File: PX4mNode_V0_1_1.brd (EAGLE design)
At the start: 48.6 x 34.9 mm, 134 parts, among them J201 DF13C-6P-1.25V, J202 DF13C-6P-1.25V, J203 DF13C-6P-1.25V, J301 DF13C-4P-1.25V, J401 DF13C-7P-1.25V, J402 DF13-4P-1.25V, J403 DF13C-4P-1.25V, J404 DF13C-4P-1.25V, J405 DF13C-4P-1.25V, J801 DF13C-3P-1.25V, M3_MOUNT1101 MOUNT-HOLE3.1MM, M3_MOUNT1102 MOUNT-HOLE3.1MM, M3_MOUNT1103 MOUNT-HOLE3.1MM, M3_MOUNT1104 MOUNT-HOLE3.1MM, U101 STM32F4X7VX, U401 MAX3051, U402 MAX3051, X101 3.2x2.5 mm / 24 MHz / 15 ppm

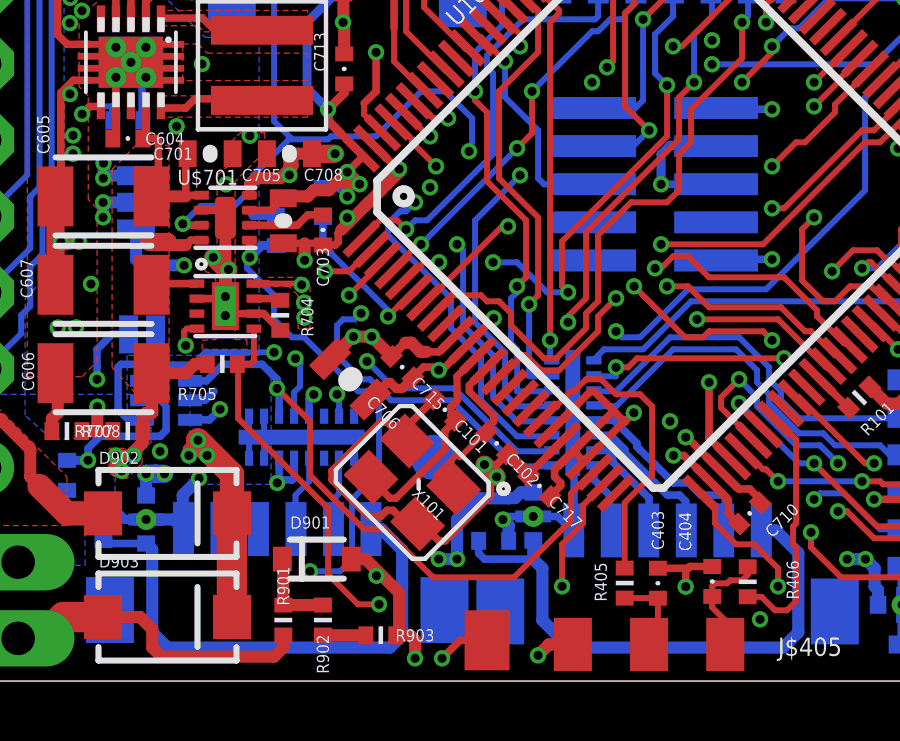
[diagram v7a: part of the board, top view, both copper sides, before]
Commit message: Reworked VBAT pullup to make psace around PSU
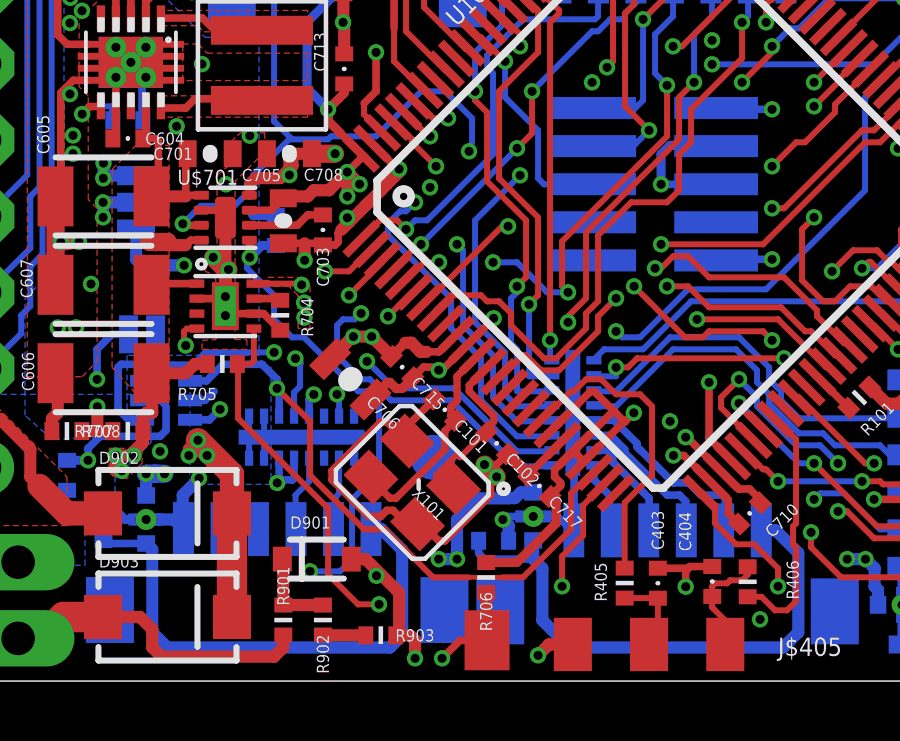
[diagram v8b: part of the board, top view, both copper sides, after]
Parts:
- moved R706 13.6 mm to (32.7, 6.19), flipped to the top
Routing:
- net FMU-VDD_3V3: track 130.4 -> 133.4 mm
- net VBAT: track 19.4 -> 16.7 mm
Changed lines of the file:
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@@
 <layer number="1" name="Top" color="4" fill="1" visible="yes" active="yes"/>
 <layer number="2" name="Ground" color="2" fill="10" visible="no" active="yes"/>
-<layer number="3" name="Horizontal" color="13" fill="15" visible="yes" active="yes"/>
+<layer number="3" name="Horizontal" color="13" fill="15" visible="no" active="yes"/>
 <layer number="4" name="Route4" color="1" fill="4" visible="no" active="no"/>
 <layer number="5" name="Route5" color="4" fill="4" visible="no" active="no"/>
@@
 <layer number="12" name="Route12" color="1" fill="5" visible="no" active="no"/>
 <layer number="13" name="Route13" color="4" fill="5" visible="no" active="no"/>
-<layer number="14" name="Vertical" color="14" fill="15" visible="yes" active="yes"/>
+<layer number="14" name="Vertical" color="14" fill="15" visible="no" active="yes"/>
 <layer number="15" name="Power" color="11" fill="15" visible="no" active="yes"/>
 <layer number="16" name="Bottom" color="1" fill="1" visible="yes" active="yes"/>
@@
 <attribute name="PARTNO" value="DF13C-4P-1.25V(20)" x="47.0408" y="33.528" size="1.778" layer="28" rot="MR180" display="off"/>
 </element>
-<element name="R706" library="pixhawk2" package="0402-RES" value="1K" x="27.2288" y="18.6944" rot="MR90">
-<attribute name="PARTNO" value="RC0402FR-071KL" x="27.2288" y="18.6944" size="1.778" layer="28" rot="MR90" display="off"/>
+<element name="R706" library="pixhawk2" package="0402-RES" value="1K" x="32.6712" y="6.1944" rot="R90">
+<attribute name="PARTNO" value="RC0402FR-071KL" x="32.6712" y="6.1944" size="1.778" layer="27" rot="R90" display="off"/>
 </element>
 <element name="C703" library="pixhawk2" package="0402-CAP" value="10n" x="27.2288" y="17.78" rot="R90">
@@
 <wire x1="35.56" y1="30.5816" x2="38.2016" y2="30.5816" width="0.4064" layer="1"/>
 <wire x1="38.2016" y1="30.5816" x2="38.2016" y2="30.6832" width="0.4064" layer="1"/>
-<wire x1="27.2288" y1="19.1944" x2="27.7448" y2="19.1944" width="0.254" layer="16"/>
-<wire x1="27.7448" y1="19.1944" x2="28.0416" y2="18.8976" width="0.254" layer="16"/>
 <wire x1="39.7256" y1="36.6776" x2="40.0304" y2="36.9824" width="0.6096" layer="1"/>
 <wire x1="40.0304" y1="36.9824" x2="40.132" y2="36.9824" width="0.6096" layer="1"/>
@@
 <wire x1="25.5" y1="22.8" x2="26.5" y2="21.8" width="0.254" layer="14"/>
 <wire x1="26.5" y1="21.8" x2="27.4" y2="21.8" width="0.254" layer="14"/>
-<wire x1="21.8" y1="10.9" x2="21.8" y2="10.4" width="0" layer="19" extent="16-16"/>
+<wire x1="21.8" y1="10.4" x2="21.8" y2="10.9" width="0" layer="19" extent="16-16"/>
+<wire x1="32.6712" y1="6.6944" x2="33.6944" y2="6.6944" width="0.3048" layer="1"/>
+<wire x1="33.6944" y1="6.6944" x2="35" y2="8" width="0.3048" layer="1"/>
+<wire x1="35" y1="8" x2="35" y2="8.687996875" width="0.3048" layer="1"/>
+<wire x1="35" y1="8.687996875" x2="34.795953125" y2="8.89204375" width="0.3048" layer="1"/>
 </signal>
 <signal name="OTG_FS_DP">
@@
 <contactref element="R706" pad="P$1"/>
 <wire x1="29.4" y1="14.9" x2="30.2" y2="15.7" width="0.2" layer="1"/>
-<wire x1="27.5" y1="17" x2="29.4" y2="15.1" width="0.2" layer="16"/>
-<wire x1="29.4" y1="15.1" x2="29.4" y2="14.9" width="0.2" layer="16"/>
 <wire x1="30.2" y1="15.7" x2="30.273071875" y2="15.71561875" width="0.2" layer="1"/>
-<wire x1="27.3" y1="18.2" x2="27.2288" y2="18.1944" width="0.2" layer="16"/>
 <via x="29.4" y="14.9" extent="1-16" drill="0.3" diameter="0.55"/>
 <contactref element="JP701" pad="P$1"/>
@@
 <wire x1="29.4" y1="14.9" x2="29.7" y2="14.6" width="0.254" layer="14"/>
 <via x="31.2" y="3.5" extent="1-16" drill="0.3"/>
-<wire x1="27.5" y1="17" x2="27.2288" y2="17.2712" width="0.254" layer="16"/>
-<wire x1="27.2288" y1="17.2712" x2="27.2288" y2="18.1944" width="0.254" layer="16"/>
+<wire x1="32.6712" y1="5.6944" x2="32.6712" y2="4.1288" width="0.4064" layer="1"/>
+<wire x1="32.6712" y1="4.1288" x2="32.7" y2="4.1" width="0.4064" layer="1"/>
 </signal>
 <signal name="N$11">
@@
 <wire x1="35.2" y1="8.7" x2="32.3" y2="11.6" width="0.2" layer="14"/>
 <wire x1="35.2" y1="5.9" x2="35.2" y2="8.7" width="0.2" layer="14"/>
-<wire x1="35.2" y1="7.3" x2="35.2" y2="5.9" width="0.2" layer="1"/>
-<wire x1="35.9" y1="8" x2="35.2" y2="7.3" width="0.2" layer="1"/>
-<wire x1="35.9" y1="8.6" x2="35.9" y2="8" width="0.2" layer="1"/>
+<wire x1="35.2" y1="6.9" x2="35.2" y2="5.9" width="0.2" layer="1"/>
+<wire x1="35.9" y1="7.6" x2="35.2" y2="6.9" width="0.2" layer="1"/>
+<wire x1="35.9" y1="8.6" x2="35.9" y2="7.6" width="0.2" layer="1"/>
 <wire x1="36.6" y1="9.3" x2="35.9" y2="8.6" width="0.2" layer="1"/>
 <wire x1="23.1" y1="28.1" x2="23.0632" y2="28.1432" width="0.2" layer="16"/>
@@
 <wire x1="29.3" y1="7.8" x2="28.6" y2="7.8" width="0.2" layer="1"/>
 <wire x1="30.9" y1="6.2" x2="29.3" y2="7.8" width="0.2" layer="1"/>
-<wire x1="33.6" y1="6.2" x2="30.9" y2="6.2" width="0.2" layer="1"/>
-<wire x1="35.5" y1="8.1" x2="33.6" y2="6.2" width="0.2" layer="1"/>
-<wire x1="35.5" y1="9" x2="35.5" y2="8.1" width="0.2" layer="1"/>
+<wire x1="33.9" y1="6.2" x2="33.2" y2="6.2" width="0.2" layer="1"/>
+<wire x1="33.2" y1="6.2" x2="32.1" y2="6.2" width="0.154" layer="1"/>
+<wire x1="32.1" y1="6.2" x2="30.9" y2="6.2" width="0.2" layer="1"/>
+<wire x1="35.5" y1="7.8" x2="33.9" y2="6.2" width="0.2" layer="1"/>
+<wire x1="35.5" y1="9" x2="35.5" y2="7.8" width="0.2" layer="1"/>
 <wire x1="36.2" y1="9.7" x2="35.5" y2="9" width="0.2" layer="1"/>
 <wire x1="26.8" y1="11.4" x2="25.6984" y2="12.4952" width="0.2" layer="1"/>
